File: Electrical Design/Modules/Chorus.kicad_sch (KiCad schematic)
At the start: 42 parts, among them Q2 2N3904, Q3 2N3904, Q4 2N3904, U3 MN3207, U8 ${SIM.PARAMS}, U9 ${SIM.PARAMS}

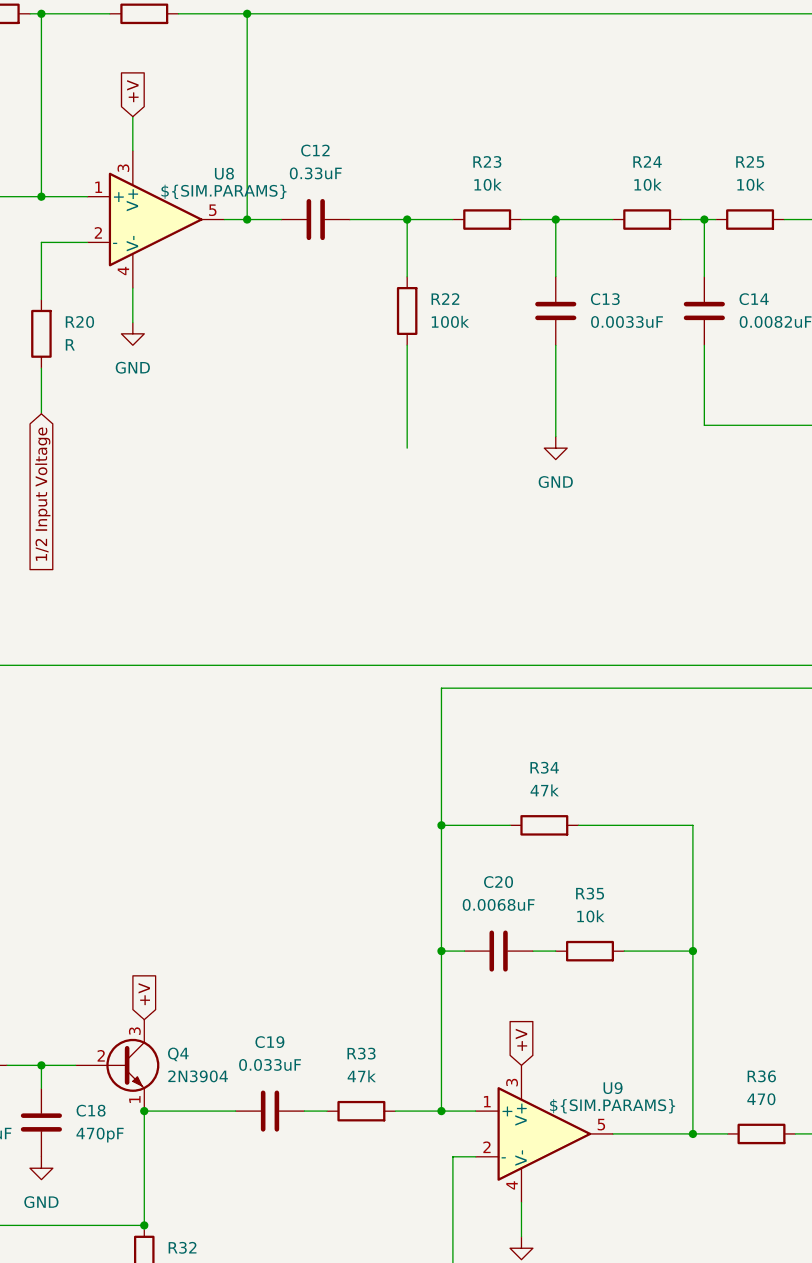
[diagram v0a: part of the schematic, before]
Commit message: Added in Specific Op amp model.
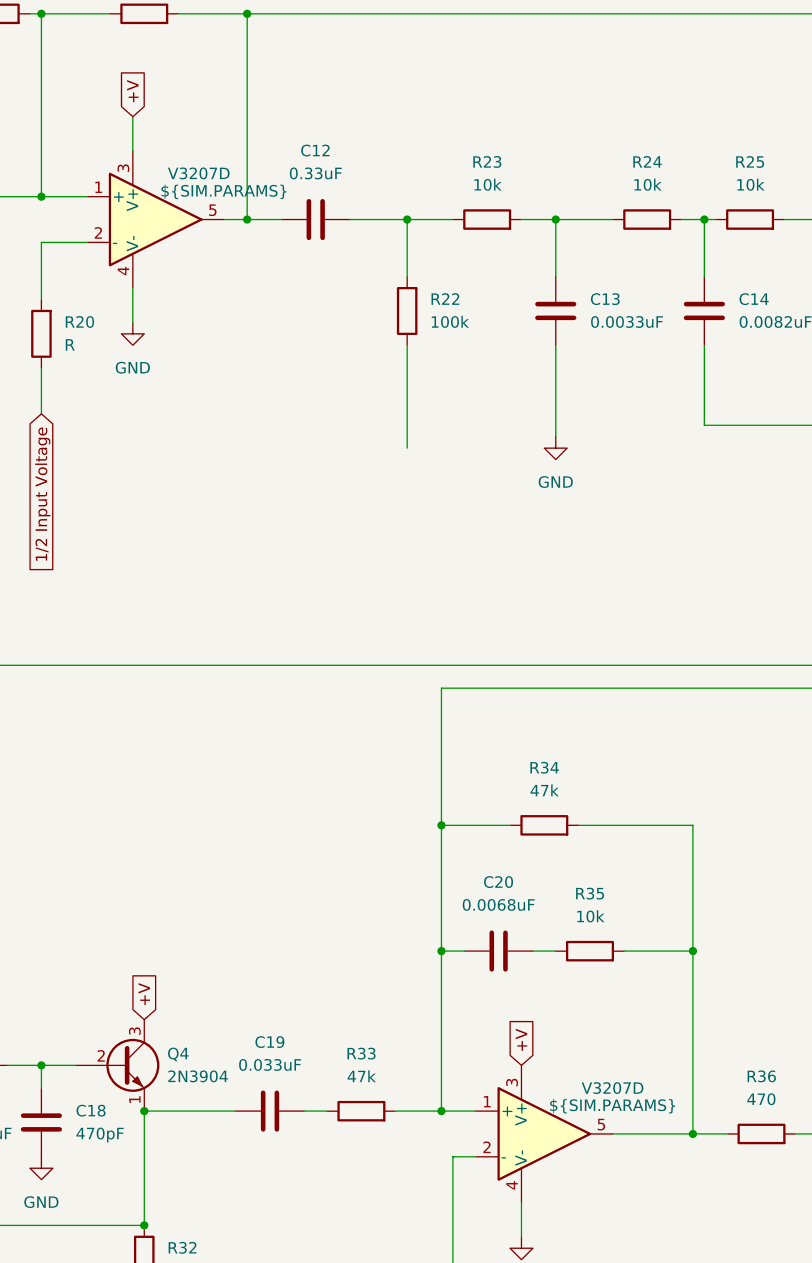
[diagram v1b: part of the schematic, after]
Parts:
- renumbered U9 to V3207D, U8 to V3207D
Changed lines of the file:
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@@
 		(dnp no)
 		(fields_autoplaced yes)
-		(property "Reference" "U9"
+		(property "Reference" "V3207D"
 			(at 156.21 141.0014 0)
 			(effects
@@
 			(project "ECE 411 Project"
 				(path "/2625e5a1-d0c8-41ce-941d-75d035a5f1c5/9b94327a-6b02-4c1c-b4e8-ca4e897770fe"
-					(reference "U9")
+					(reference "V3207D")
 					(unit 1)
 				)
@@
 		(on_board yes)
 		(dnp no)
-		(fields_autoplaced yes)
-		(property "Reference" "U8"
-			(at 113.03 39.4014 0)
+		(property "Reference" "V3207D"
+			(at 110.236 39.37 0)
 			(effects
 				(font
@@
 			(project ""
 				(path "/2625e5a1-d0c8-41ce-941d-75d035a5f1c5/9b94327a-6b02-4c1c-b4e8-ca4e897770fe"
-					(reference "U8")
-					(unit 1)
-				)
+					(reference "V3207D")
+					(unit 1)
+				)
